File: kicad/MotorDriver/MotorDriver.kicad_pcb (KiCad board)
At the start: 4 copper layers, 78 x 69.6 mm, 107 parts, among them J1 Conn_01x03_Pin, J2 Conn_01x06_Pin, J3 Conn_01x02_Pin, J4 Conn_01x02_Socket, J5 Conn_01x03_Socket, U1 STM32F446RETx, U2 ATA6560-GAQW, U3 AS5147U, U4 DRV8323RSRGZR, U5 CSD88599Q5DC, U6 CSD88599Q5DC, U8 CSD88599Q5DC, Y2 ABL-8.000MHZ-B1U-T

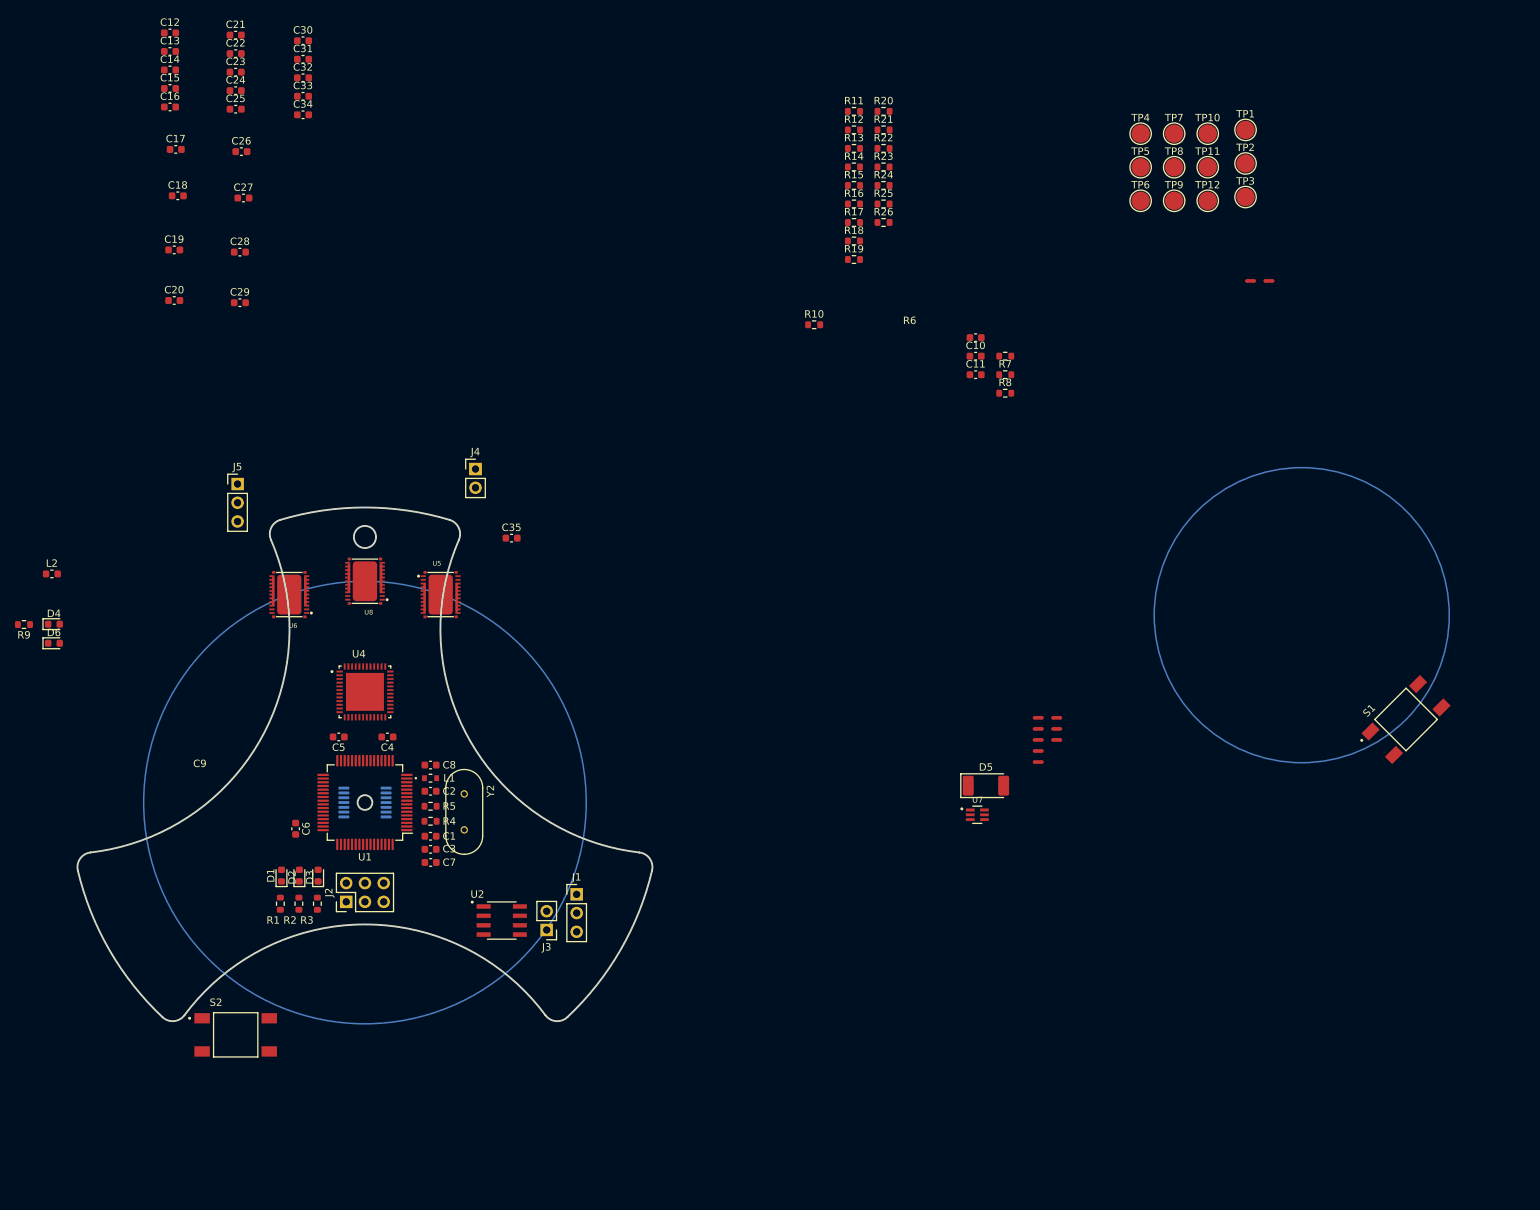
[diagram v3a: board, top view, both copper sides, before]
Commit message: Updated the planetary gearbox design. It is much better with retaining rings and bearing support. 95% done with the PCB routing. Need to just do a final routing check and i think I can put the order in
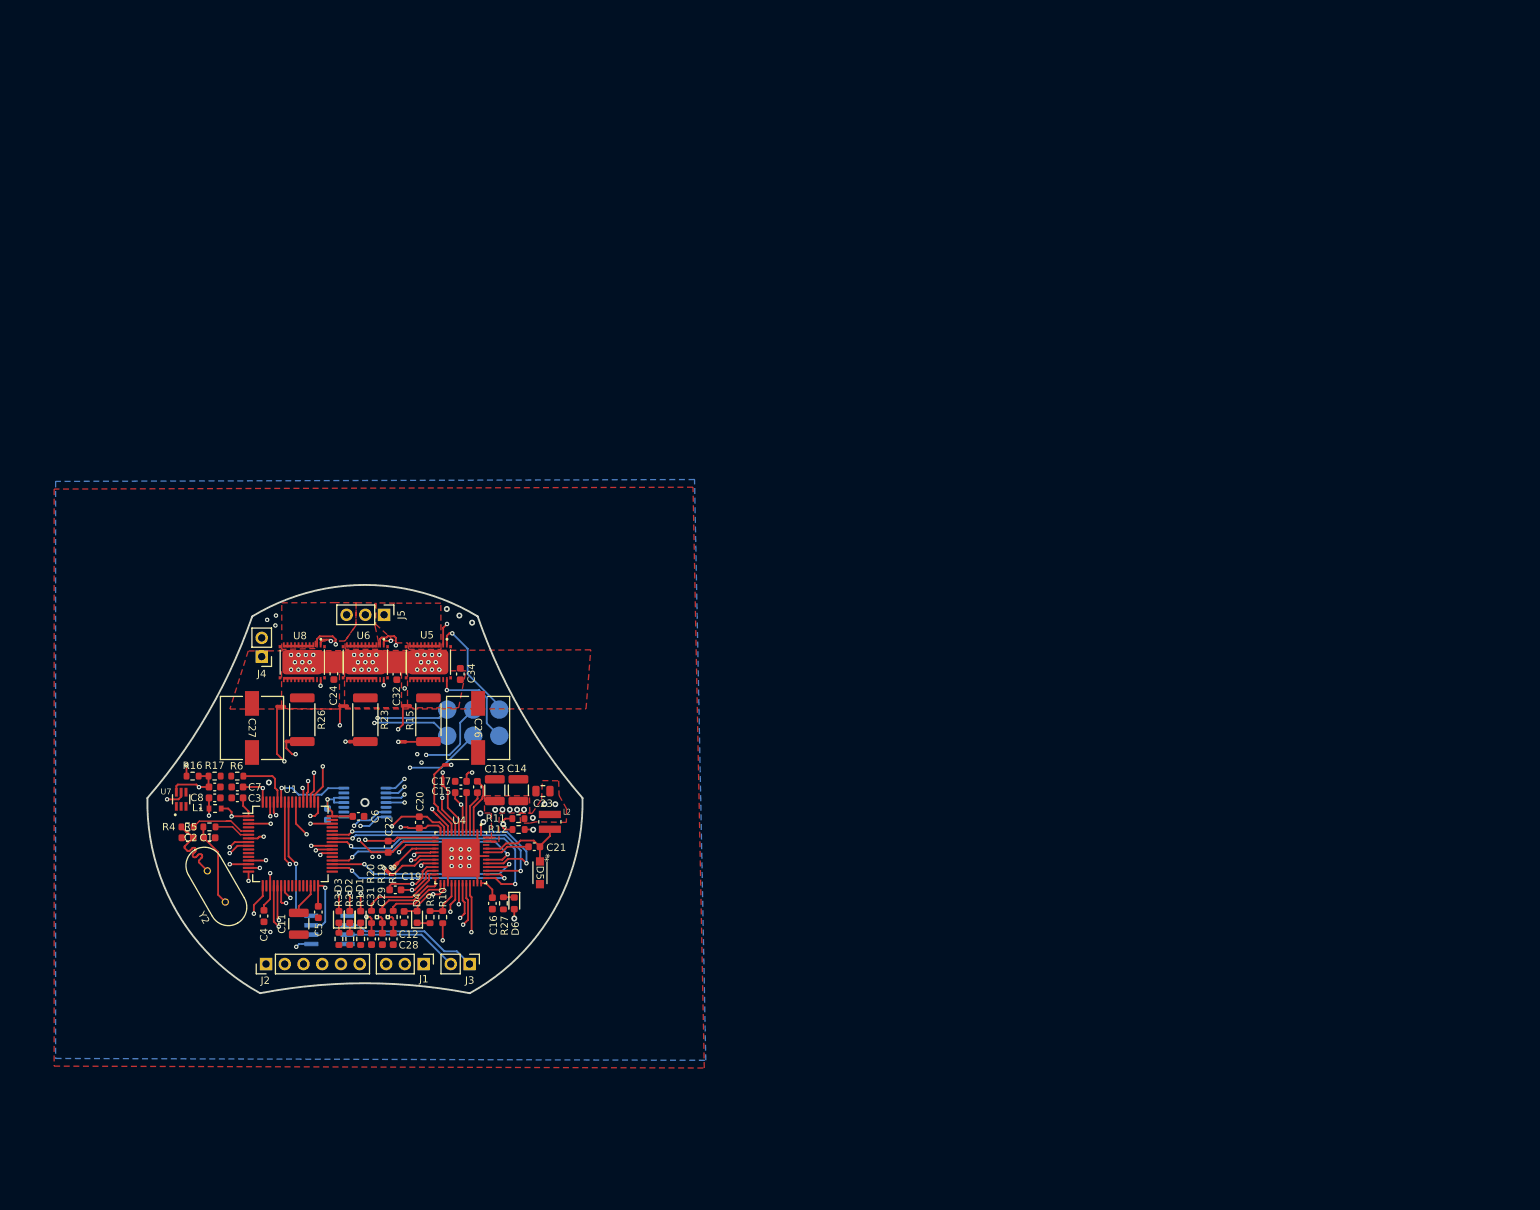
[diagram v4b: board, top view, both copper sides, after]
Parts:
- removed C25, C33, C35: 0.1 uF, Capacitor_SMD:C_0603_1608Metric
- removed C9: 4.7uF, Capacitor_SMD:C_0603_1608Metric
- removed R13, R21, R24: 82.0k, Resistor_SMD:R_0603_1608Metric
- removed R14, R22, R25: 4.99k, Resistor_SMD:R_0603_1608Metric
- removed R7: 4.7k, Resistor_SMD:R_0603_1608Metric
- removed R8: 100, Resistor_SMD:R_0603_1608Metric
- removed S1, S2: TS04-66-75-BK-160-SMT, TylerLib:SW_TS04-66-75-BK-160-SMT
- removed TP1, TP10, TP2, TP3, TP4, TP7: TestPoint, TestPoint:TestPoint_Pad_D2.5mm
- added R27: 330, Resistor_SMD:R_0603_1608Metric, F.Cu at (102.6, 148.3)
- C10, TP11, TP12, TP5, TP6, TP8, TP9, U2: moved to B.Cu
- C11: value 100nF -> 4.7uF; footprint Capacitor_SMD:C_0603_1608Metric -> Capacitor_SMD:C_1210_3225Metric
- C13, C14: footprint Capacitor_SMD:C_0603_1608Metric -> Capacitor_SMD:C_1210_3225Metric
- C23: footprint Capacitor_SMD:C_0603_1608Metric -> Capacitor_SMD:C_0805_2012Metric
- C26, C27: value 330uF -> 220uF; footprint Capacitor_SMD:C_0603_1608Metric -> TylerLib:CHEMI-HA0
- D5: value MBR1H100SFT3G -> NRVB1H100SFT3G; footprint Diode_SMD:D_MELF -> TylerLib:DIODE_SOD123LF_2P9X1P8_ONS
- J2: footprint Connector_PinHeader_2.54mm:PinHeader_2x03_P2.54mm_Vertical -> Connector_PinHeader_2.54mm:PinHeader_1x06_P2.54mm_Vertical
- L2: footprint Inductor_SMD:L_0603_1608Metric -> TylerLib:IND_VLS3015CX-150M-1
- R15, R23, R26: footprint Resistor_SMD:R_0603_1608Metric -> Resistor_SMD:R_2512_6332Metric
- moved NT7 142.6 mm to (87.9, 143.2), turned to 45 degrees
- moved R20 129.4 mm to (84.7, 150.1), turned to -90 degrees
- moved NT1 128.1 mm to (89.5, 121.5)
- moved TP11 126.6 mm to (95.0, 122.0), turned to 180 degrees
- moved TP12 126.1 mm to (95.0, 125.6), turned to 180 degrees
- moved C12 124.0 mm to (89.1, 150.2), turned to -90 degrees
- moved TP8 120.2 mm to (98.5, 122.0), turned to 180 degrees
- moved C31 119.6 mm to (84.7, 153.1), turned to -90 degrees
- moved TP9 119.5 mm to (98.5, 125.6), turned to 180 degrees
- moved R6 118.7 mm to (66.5, 131.0), turned to 180 degrees
- moved R16 118.6 mm to (60.5, 131.0)
- moved C11 118.2 mm to (74.9, 151.1), turned to 90 degrees
- moved C21 117.2 mm to (106.8, 140.6)
- moved C16 116.5 mm to (101.1, 148.3), turned to -90 degrees
- moved R17 114.7 mm to (63.4, 131.0)
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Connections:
- net Net-(U1-PH0) renamed /Microcontroller/CLK_P
- net Net-(U1-PH1) renamed /Microcontroller/CLK_N
- C10 pad 1: Net-(C10-Pad1) -> GND
- C10 pad 2: /Microcontroller/NRST -> +3.3V
- C11 pad 1: Net-(C11-Pad1) -> GND
- C11 pad 2: /Microcontroller/Button -> Net-(U1-VCAP_1)
- C26 pad 1: Net-(J4-Pin_1) -> Vdrive
- C27 pad 1: Net-(J4-Pin_1) -> Vdrive
- C28 pad 1: /MotorController/ISENA -> /Microcontroller/SEN.ISENA
- C29 pad 1: /MotorController/ISENB -> /Microcontroller/SEN.ISENB
- C30 pad 1: /MotorController/SEN.VSENVM -> /Microcontroller/SEN.VSENVM
- C31 pad 1: /MotorController/ISENC -> /Microcontroller/SEN.ISENC
- D6 pad 1: GND -> Net-(D6-K)
- J4 pad 1: Net-(J4-Pin_1) -> Vdrive
- R16 pad 1: Net-(J4-Pin_1) -> Vdrive
- R16 pad 2: /MotorController/SEN.VSENVM -> /Microcontroller/SEN.VSENVM
- R17 pad 1: /MotorController/SEN.VSENVM -> /Microcontroller/SEN.VSENVM
- R18 pad 2: /MotorController/ISENA -> /Microcontroller/SEN.ISENA
- R19 pad 2: /MotorController/ISENB -> /Microcontroller/SEN.ISENB
- R20 pad 2: /MotorController/ISENC -> /Microcontroller/SEN.ISENC
- U1 pad 14: /Microcontroller/SEN.SOA -> /Microcontroller/SEN.ISENA
- U1 pad 34: /Microcontroller/DRV.INHA -> /Microcontroller/DRV.INLA
- U1 pad 35: /Microcontroller/DRV.INHB -> /Microcontroller/DRV.INLB
- U1 pad 36: /Microcontroller/DRV.INHC -> /Microcontroller/DRV.INLC
- U1 pad 8: /Microcontroller/SEN.SOC -> /Microcontroller/SEN.ISENC
- U1 pad 9: /Microcontroller/SEN.SOB -> /Microcontroller/SEN.ISENB
- U4 pad 23: /MotorController/SEN.SOC -> /MotorController/SOC
- U4 pad 24: /MotorController/SEN.SOB -> /MotorController/SOB
- U4 pad 25: /MotorController/SEN.SOA -> /MotorController/SOA
- U4 pad 29: /MotorController/SPI1.MISO -> /Microcontroller/SPI1.MISO
- U4 pad 30: /MotorController/SPI1.MOSI -> /Microcontroller/SPI1.MOSI
- U4 pad 31: /MotorController/SPI1.SCK -> /Microcontroller/SPI1.SCK
- U4 pad 32: /MotorController/SPI1.CS -> /Microcontroller/SPI1.CS
- U7 pad 1: /MotorController/VSENA -> unconnected-(U7-D1+-Pad1)
- U7 pad 3: /MotorController/VSENB -> unconnected-(U7-D2+-Pad3)
- U7 pad 4: /MotorController/VSENC -> unconnected-(U7-D2--Pad4)
- U7 pad 6: /MotorController/VSENVM -> /Microcontroller/SEN.VSENVM
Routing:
- net /MotorController/GHC: track 0.00 -> 55.1 mm, vias 0 -> 4
- net /Microcontroller/DRV.ENABLE: track 0.00 -> 53.4 mm, vias 0 -> 3
- net +3.3V: track 0.00 -> 52.9 mm, vias 0 -> 12
- net /MotorController/SPC: track 0.00 -> 52.4 mm, vias 0 -> 3
- net /MotorController/GLC: track 0.00 -> 50.2 mm, vias 0 -> 4
- net /MotorController/GHB: track 0.00 -> 47.4 mm, vias 0 -> 3
- net /MotorController/SNC: track 0.00 -> 44.8 mm, vias 0 -> 3
- net /MotorController/GHA: track 0.00 -> 43.9 mm, vias 0 -> 2
- net /MotorController/GLB: track 0.00 -> 42.6 mm, vias 0 -> 4
- net Net-(U8-SH): track 0.00 -> 40.3 mm, vias 0 -> 2
- net /Microcontroller/SPI1.CS: track 0.00 -> 37.8 mm, vias 0 -> 2
- net /Microcontroller/SPI1.SCK: track 0.00 -> 35.4 mm, vias 0 -> 2
- net /Microcontroller/DRV.INHA: track 0.00 -> 35.3 mm, vias 0 -> 2
- net /Microcontroller/DRV.INHC: track 0.00 -> 35.2 mm, vias 0 -> 2
- net Net-(U6-SH): track 0.00 -> 35.2 mm, vias 0 -> 2
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- added copper zone on F.Cu, net +3.3V
- added copper zone on In1.Cu, net +3.3V
- added copper zone on F.Cu, net /MotorController/MOTA
- added copper zone on F.Cu, net /MotorController/MOTB
- added copper zone on F.Cu, net /MotorController/MOTC
- added copper zone on F.Cu, net /MotorController/SLA
- added copper zone on F.Cu, net /MotorController/SLB
- added copper zone on F.Cu, net /MotorController/SLC
- added copper zone on B.Cu, net GND
- added copper zone on F.Cu, net GND
- added copper zone on In1.Cu, net GND
- added copper zone on In2.Cu, net GND
- added copper zone on F.Cu, net Vdrive
- added copper zone on In1.Cu, net Vdrive
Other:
- board size 78 x 69.6 mm -> 59 x 55.3 mm

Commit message: PCB ordered
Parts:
- removed D1, D2, D3: LED, LED_SMD:LED_0603_1608Metric
- removed R4, R5: 80, Resistor_SMD:R_0603_1608Metric
- added U9: 150066M153000, TylerLib:CHIP_M153000_WRE, F.Cu at (81.7, 153.2)
- C10, C3, C4, C5, C6, C7, C8: value 100nF -> 0.1uF
- C24, C34: value 0.01 uF -> 10000pF
- C32: value 0.01 uF -> 10000 pF
- D4: value LED -> RedLED
- D6: value LED -> BlueLED
- R1: value 1k -> 330
- U7: value ~ -> TPD4S009DCKR
- moved R1 2.97 mm to (83.2, 150.1)
- moved R2 2.97 mm to (81.8, 150.1)
- moved R3 2.97 mm to (80.3, 150.1)
- moved NT2 1.89 mm to (90.7, 126.4)
- turned C1 to 180 degrees
- turned C2 to 0 degrees
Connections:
- C1 pad 2: Net-(C1-Pad2) -> /Microcontroller/CLK_P
- C2 pad 2: Net-(C2-Pad2) -> /Microcontroller/CLK_N
- R1 pad 1: Net-(D1-K) -> Net-(U1-PC6)
- R1 pad 2: GND -> Net-(R1-Pad2)
- R2 pad 1: Net-(D2-K) -> Net-(U1-PC7)
- R2 pad 2: GND -> Net-(R2-Pad2)
- R3 pad 1: Net-(D3-K) -> Net-(U1-PC8)
- R3 pad 2: GND -> Net-(R3-Pad2)
- U1 pad 37: unconnected-(U1-PC6-Pad37) -> Net-(U1-PC6)
- U1 pad 38: Net-(D1-A) -> Net-(U1-PC7)
- U1 pad 39: Net-(D2-A) -> Net-(U1-PC8)
- U1 pad 40: Net-(D3-A) -> unconnected-(U1-PC9-Pad40)
- Y2 pad 1: Net-(C2-Pad2) -> /Microcontroller/CLK_N
- Y2 pad 2: Net-(C1-Pad2) -> /Microcontroller/CLK_P
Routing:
- net Vdrive: track 31.5 -> 45.8 mm, vias 42 -> 55
- net Net-(D3-A): track 13.3 -> 0.00 mm, vias 2 -> 0
- net Net-(U1-PC8): track 0.00 -> 13.3 mm, vias 0 -> 2
- net Net-(D2-A): track 12.9 -> 0.00 mm, vias 2 -> 0
- net Net-(D1-A): track 12.5 -> 0.00 mm, vias 2 -> 0
- net Net-(U1-PC7): track 0.00 -> 12.5 mm, vias 0 -> 2
- net Net-(U1-PC6): track 0.00 -> 12.0 mm, vias 0 -> 2
- net Net-(C2-Pad2): track 11.4 -> 0.00 mm
- net Net-(C1-Pad2): track 11.4 -> 0.00 mm
- net /Microcontroller/CLK_N: track 4.91 -> 14.0 mm
- net /Microcontroller/CLK_P: track 8.87 -> 15.3 mm
- net Net-(R3-Pad2): track 0.00 -> 3.36 mm
- net +3.3V: track 52.9 -> 56.0 mm
- net /MotorController/SPA: track 25.9 -> 22.8 mm
- net GND: track 20.7 -> 17.7 mm, vias 18 -> 55
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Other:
- outline, holes or cut-outs redrawn

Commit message: Working on some of the solidworks model, new urdf, working on the motor drive board a little
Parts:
- removed Y2: ABL-8.000MHZ-B1U-T, TylerLib:XTAL_ABL-8.000MHZ-B1U-T
- added TP1: TestPoint, TestPoint:TestPoint_Pad_D1.0mm, B.Cu at (77.0, 125.2)
- added TP10: TestPoint, TestPoint:TestPoint_Pad_D1.0mm, B.Cu at (91.2, 136.2)
- added TP13: TestPoint, TestPoint:TestPoint_Pad_D1.0mm, B.Cu at (81.0, 130.4)
- added TP14: TestPoint, TestPoint:TestPoint_Pad_D1.0mm, B.Cu at (100.4, 141.2)
- added TP15: TestPoint, TestPoint:TestPoint_Pad_D1.0mm, B.Cu at (107.8, 142.8)
- added TP16: TestPoint, TestPoint:TestPoint_Pad_D1.0mm, B.Cu at (100.4, 143.2)
- added TP17: TestPoint, TestPoint:TestPoint_Pad_D1.0mm, B.Cu at (107.8, 144.9)
- added TP18: TestPoint, TestPoint:TestPoint_Pad_D1.0mm, B.Cu at (105.7, 147.1)
- added TP19: TestPoint, TestPoint:TestPoint_Pad_D1.0mm, B.Cu at (107.9, 147.0)
- added TP2: TestPoint, TestPoint:TestPoint_Pad_D1.0mm, B.Cu at (77.0, 127.3)
- added TP3: TestPoint, TestPoint:TestPoint_Pad_D1.0mm, B.Cu at (74.9, 127.2)
- added TP4: TestPoint, TestPoint:TestPoint_Pad_D1.0mm, B.Cu at (74.9, 125.1)
- added TP7: TestPoint, TestPoint:TestPoint_Pad_D1.0mm, B.Cu at (91.2, 134.2)
- added Y1: 406I35D08M00000, TylerLib:XTAL_406I35D08M00000, F.Cu at (62.0, 142.0)
- TP11, TP12, TP5, TP6, TP8, TP9: footprint TestPoint:TestPoint_Pad_D2.5mm -> TestPoint:TestPoint_Pad_D1.0mm
- moved C2 6.85 mm to (64.0, 146.1), turned to 180 degrees
- moved C1 1.57 mm to (60.0, 137.8), turned to 0 degrees
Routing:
- net /Encoder/SPI3.MOSI: track 18.0 -> 26.1 mm
- net /Microcontroller/CLK_P: track 15.3 -> 9.74 mm
- net /Encoder/M1_ENC.B: track 20.0 -> 25.2 mm
- net /Encoder/SPI3.CS: track 18.6 -> 23.6 mm
- net /Encoder/SPI3.MISO: track 17.7 -> 22.7 mm
- net /Encoder/M1_ENC.A: track 19.1 -> 24.1 mm
- net /Microcontroller/DRV.INHA: track 35.3 -> 39.5 mm
- net /Microcontroller/DRV.INLA: track 26.6 -> 30.6 mm
- net /Microcontroller/CLK_N: track 14.0 -> 10.5 mm
- net /Encoder/SPI3.SCK: track 18.5 -> 21.8 mm
- net /Microcontroller/DRV.INHB: track 34.1 -> 37.4 mm
- net /Encoder/M1_ENC.I: track 11.1 -> 13.3 mm
- net /Microcontroller/DRV.INHC: track 35.2 -> 37.4 mm
- net /Microcontroller/DRV.INLC: track 28.8 -> 30.0 mm
- net /Microcontroller/DRV.INLB: track 28.4 -> 29.5 mm
